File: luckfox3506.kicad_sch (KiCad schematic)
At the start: 3 parts, among them J1 Conn_01x60, J2 Conn_01x60

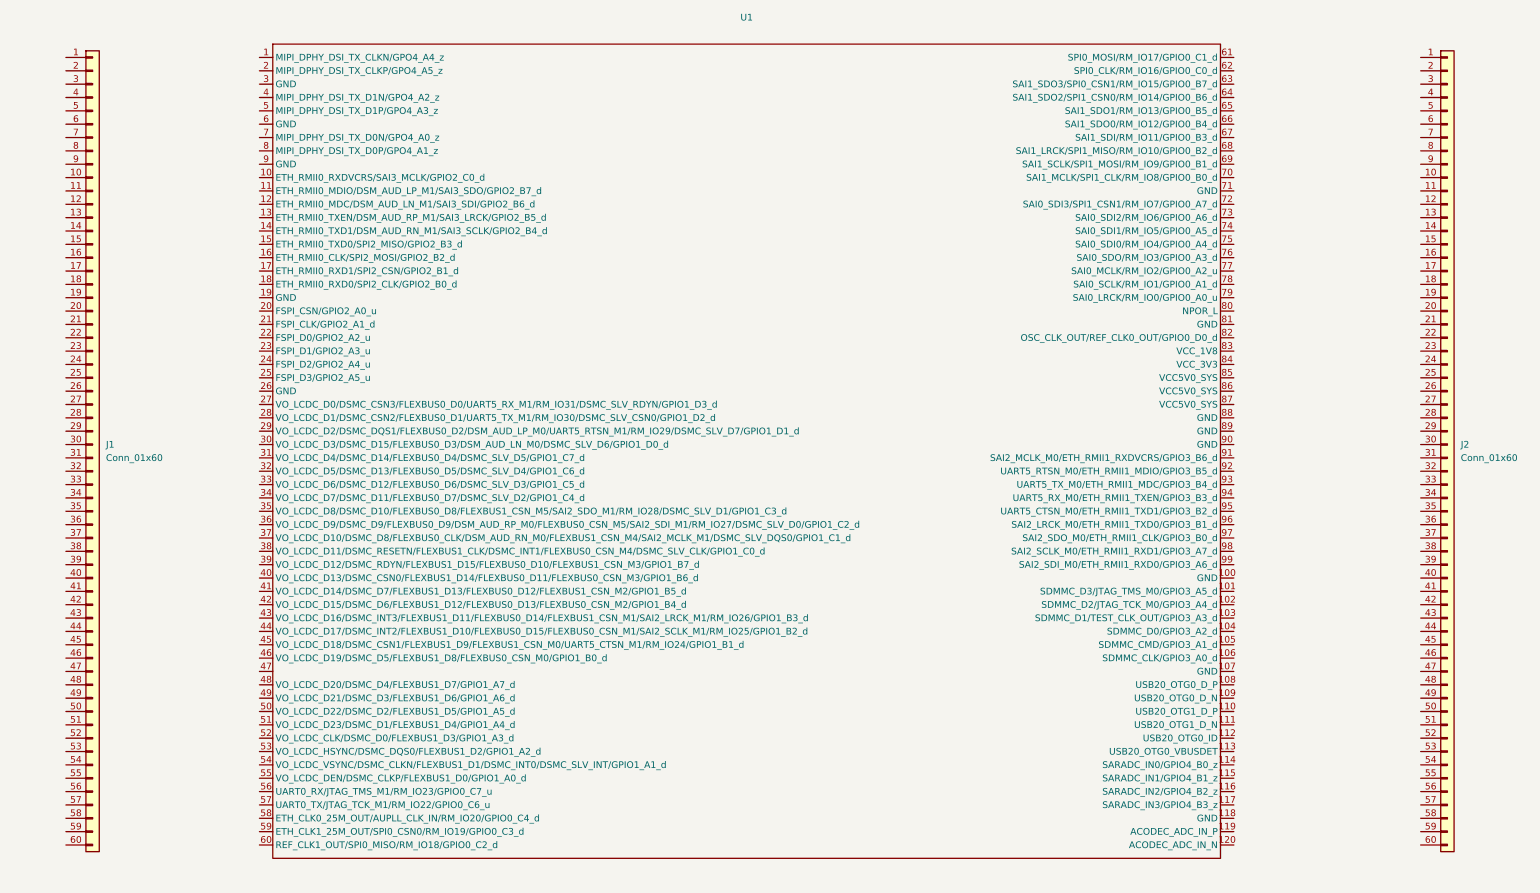
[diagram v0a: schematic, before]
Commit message: Added footprints for headers
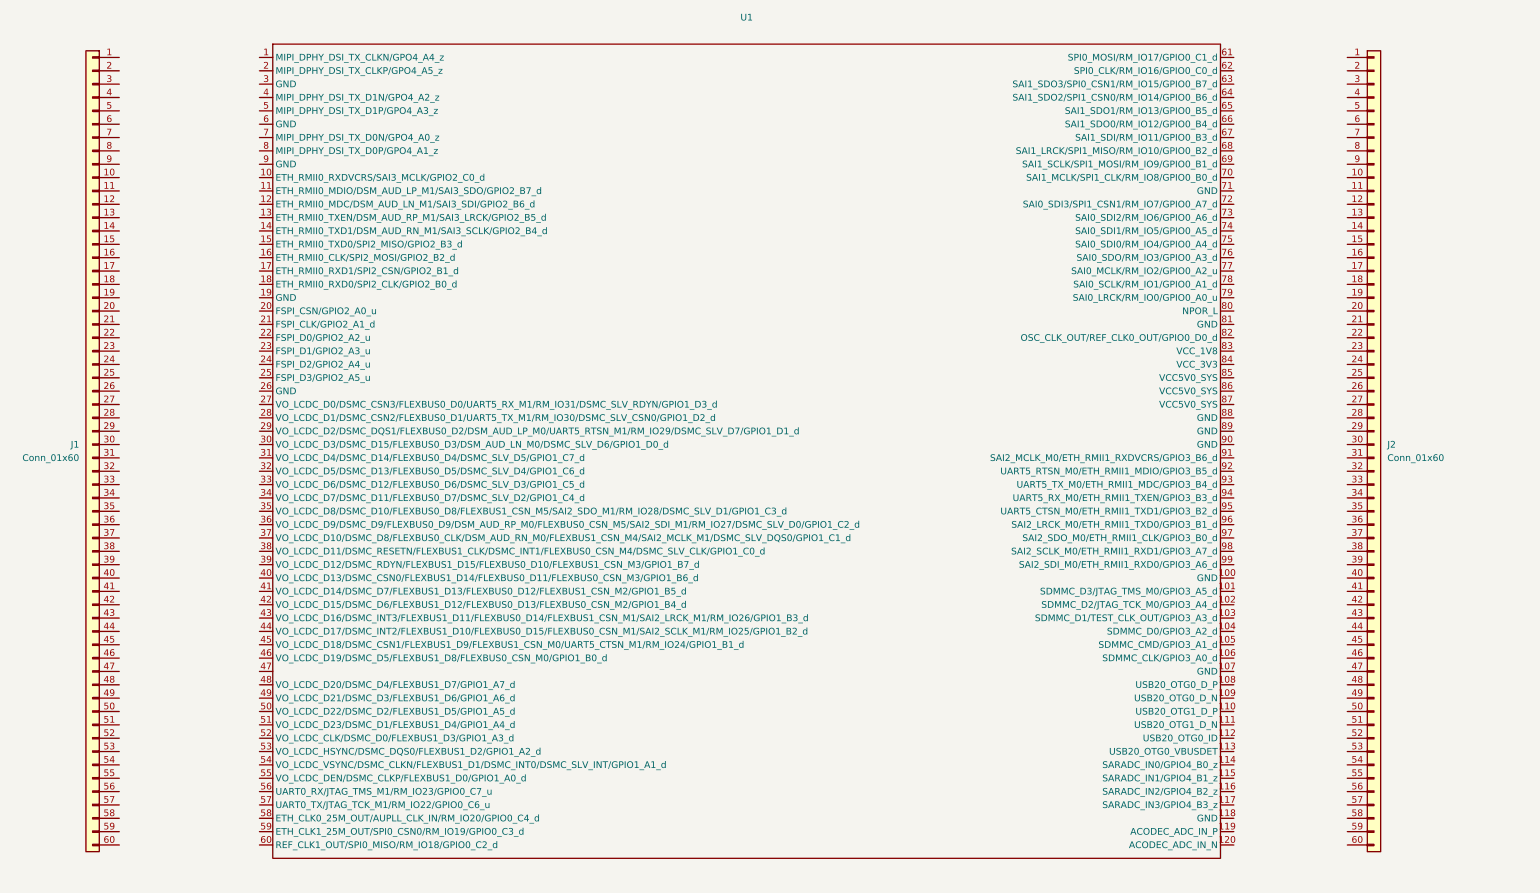
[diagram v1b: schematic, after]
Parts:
- J1, J2: footprint (none) -> Library:PinHeader_1x60_P2.54mm_Vertical
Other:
- moved on the sheet: J1

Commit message: Added nets
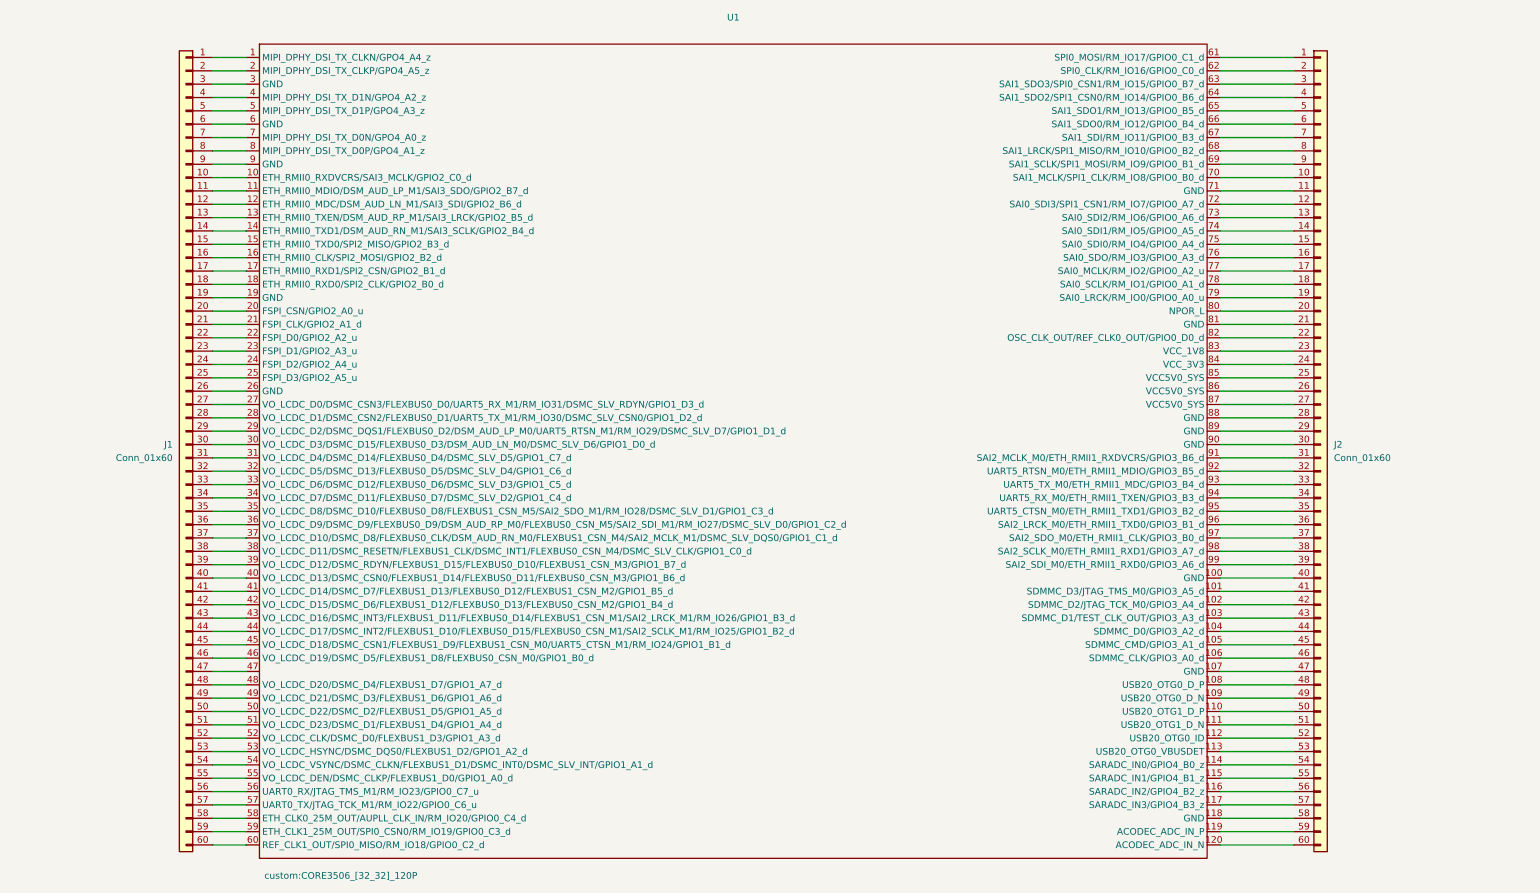
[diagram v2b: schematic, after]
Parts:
- U1: footprint Core3506:CORE3506_[32_32]_120P -> custom:CORE3506_[32_32]_120P
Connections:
- net at J1.1 (Pin_1): now also U1.1 (MIPI_DPHY_DSI_TX_CLKN/GPO4_A4_z)
- net at J1.10 (Pin_10): now also U1.10 (ETH_RMII0_RXDVCRS/SAI3_MCLK/GPIO2_C0_d)
- net at J1.11 (Pin_11): now also U1.11 (ETH_RMII0_MDIO/DSM_AUD_LP_M1/SAI3_SDO/GPIO2_B7_d)
- net at J1.12 (Pin_12): now also U1.12 (ETH_RMII0_MDC/DSM_AUD_LN_M1/SAI3_SDI/GPIO2_B6_d)
- net at J1.13 (Pin_13): now also U1.13 (ETH_RMII0_TXEN/DSM_AUD_RP_M1/SAI3_LRCK/GPIO2_B5_d)
- net at J1.14 (Pin_14): now also U1.14 (ETH_RMII0_TXD1/DSM_AUD_RN_M1/SAI3_SCLK/GPIO2_B4_d)
- net at J1.15 (Pin_15): now also U1.15 (ETH_RMII0_TXD0/SPI2_MISO/GPIO2_B3_d)
- net at J1.16 (Pin_16): now also U1.16 (ETH_RMII0_CLK/SPI2_MOSI/GPIO2_B2_d)
- net at J1.17 (Pin_17): now also U1.17 (ETH_RMII0_RXD1/SPI2_CSN/GPIO2_B1_d)
- net at J1.18 (Pin_18): now also U1.18 (ETH_RMII0_RXD0/SPI2_CLK/GPIO2_B0_d)
- net at J1.19 (Pin_19): now also U1.19 (GND)
- net at J1.2 (Pin_2): now also U1.2 (MIPI_DPHY_DSI_TX_CLKP/GPO4_A5_z)
- net at J1.20 (Pin_20): now also U1.20 (FSPI_CSN/GPIO2_A0_u)
- net at J1.21 (Pin_21): now also U1.21 (FSPI_CLK/GPIO2_A1_d)
- net at J1.22 (Pin_22): now also U1.22 (FSPI_D0/GPIO2_A2_u)
- net at J1.23 (Pin_23): now also U1.23 (FSPI_D1/GPIO2_A3_u)
- net at J1.24 (Pin_24): now also U1.24 (FSPI_D2/GPIO2_A4_u)
- net at J1.25 (Pin_25): now also U1.25 (FSPI_D3/GPIO2_A5_u)
- net at J1.26 (Pin_26): now also U1.26 (GND)
- net at J1.27 (Pin_27): now also U1.27 (VO_LCDC_D0/DSMC_CSN3/FLEXBUS0_D0/UART5_RX_M1/RM_IO31/DSMC_SLV_RDYN/GPIO1_D3_d)
- net at J1.28 (Pin_28): now also U1.28 (VO_LCDC_D1/DSMC_CSN2/FLEXBUS0_D1/UART5_TX_M1/RM_IO30/DSMC_SLV_CSN0/GPIO1_D2_d)
- net at J1.29 (Pin_29): now also U1.29 (VO_LCDC_D2/DSMC_DQS1/FLEXBUS0_D2/DSM_AUD_LP_M0/UART5_RTSN_M1/RM_IO29/DSMC_SLV_D7/GPIO1_D1_d)
- net at J1.3 (Pin_3): now also U1.3 (GND)
- net at J1.30 (Pin_30): now also U1.30 (VO_LCDC_D3/DSMC_D15/FLEXBUS0_D3/DSM_AUD_LN_M0/DSMC_SLV_D6/GPIO1_D0_d)
- net at J1.31 (Pin_31): now also U1.31 (VO_LCDC_D4/DSMC_D14/FLEXBUS0_D4/DSMC_SLV_D5/GPIO1_C7_d)
- net at J1.32 (Pin_32): now also U1.32 (VO_LCDC_D5/DSMC_D13/FLEXBUS0_D5/DSMC_SLV_D4/GPIO1_C6_d)
- net at J1.33 (Pin_33): now also U1.33 (VO_LCDC_D6/DSMC_D12/FLEXBUS0_D6/DSMC_SLV_D3/GPIO1_C5_d)
- net at J1.34 (Pin_34): now also U1.34 (VO_LCDC_D7/DSMC_D11/FLEXBUS0_D7/DSMC_SLV_D2/GPIO1_C4_d)
- net at J1.35 (Pin_35): now also U1.35 (VO_LCDC_D8/DSMC_D10/FLEXBUS0_D8/FLEXBUS1_CSN_M5/SAI2_SDO_M1/RM_IO28/DSMC_SLV_D1/GPIO1_C3_d)
- net at J1.36 (Pin_36): now also U1.36 (VO_LCDC_D9/DSMC_D9/FLEXBUS0_D9/DSM_AUD_RP_M0/FLEXBUS0_CSN_M5/SAI2_SDI_M1/RM_IO27/DSMC_SLV_D0/GPIO1_C2_d)
- net at J1.37 (Pin_37): now also U1.37 (VO_LCDC_D10/DSMC_D8/FLEXBUS0_CLK/DSM_AUD_RN_M0/FLEXBUS1_CSN_M4/SAI2_MCLK_M1/DSMC_SLV_DQS0/GPIO1_C1_d)
- net at J1.38 (Pin_38): now also U1.38 (VO_LCDC_D11/DSMC_RESETN/FLEXBUS1_CLK/DSMC_INT1/FLEXBUS0_CSN_M4/DSMC_SLV_CLK/GPIO1_C0_d)
- net at J1.39 (Pin_39): now also U1.39 (VO_LCDC_D12/DSMC_RDYN/FLEXBUS1_D15/FLEXBUS0_D10/FLEXBUS1_CSN_M3/GPIO1_B7_d)
- net at J1.4 (Pin_4): now also U1.4 (MIPI_DPHY_DSI_TX_D1N/GPO4_A2_z)
- net at J1.40 (Pin_40): now also U1.40 (VO_LCDC_D13/DSMC_CSN0/FLEXBUS1_D14/FLEXBUS0_D11/FLEXBUS0_CSN_M3/GPIO1_B6_d)
- net at J1.41 (Pin_41): now also U1.41 (VO_LCDC_D14/DSMC_D7/FLEXBUS1_D13/FLEXBUS0_D12/FLEXBUS1_CSN_M2/GPIO1_B5_d)
- net at J1.42 (Pin_42): now also U1.42 (VO_LCDC_D15/DSMC_D6/FLEXBUS1_D12/FLEXBUS0_D13/FLEXBUS0_CSN_M2/GPIO1_B4_d)
- net at J1.43 (Pin_43): now also U1.43 (VO_LCDC_D16/DSMC_INT3/FLEXBUS1_D11/FLEXBUS0_D14/FLEXBUS1_CSN_M1/SAI2_LRCK_M1/RM_IO26/GPIO1_B3_d)
- net at J1.44 (Pin_44): now also U1.44 (VO_LCDC_D17/DSMC_INT2/FLEXBUS1_D10/FLEXBUS0_D15/FLEXBUS0_CSN_M1/SAI2_SCLK_M1/RM_IO25/GPIO1_B2_d)
- net at J1.45 (Pin_45): now also U1.45 (VO_LCDC_D18/DSMC_CSN1/FLEXBUS1_D9/FLEXBUS1_CSN_M0/UART5_CTSN_M1/RM_IO24/GPIO1_B1_d)
- net at J1.46 (Pin_46): now also U1.46 (VO_LCDC_D19/DSMC_D5/FLEXBUS1_D8/FLEXBUS0_CSN_M0/GPIO1_B0_d)
- net at J1.47 (Pin_47): now also U1.47
- net at J1.48 (Pin_48): now also U1.48 (VO_LCDC_D20/DSMC_D4/FLEXBUS1_D7/GPIO1_A7_d)
- net at J1.49 (Pin_49): now also U1.49 (VO_LCDC_D21/DSMC_D3/FLEXBUS1_D6/GPIO1_A6_d)
- net at J1.5 (Pin_5): now also U1.5 (MIPI_DPHY_DSI_TX_D1P/GPO4_A3_z)
- net at J1.50 (Pin_50): now also U1.50 (VO_LCDC_D22/DSMC_D2/FLEXBUS1_D5/GPIO1_A5_d)
- net at J1.51 (Pin_51): now also U1.51 (VO_LCDC_D23/DSMC_D1/FLEXBUS1_D4/GPIO1_A4_d)
- net at J1.52 (Pin_52): now also U1.52 (VO_LCDC_CLK/DSMC_D0/FLEXBUS1_D3/GPIO1_A3_d)
- net at J1.53 (Pin_53): now also U1.53 (VO_LCDC_HSYNC/DSMC_DQS0/FLEXBUS1_D2/GPIO1_A2_d)
- net at J1.54 (Pin_54): now also U1.54 (VO_LCDC_VSYNC/DSMC_CLKN/FLEXBUS1_D1/DSMC_INT0/DSMC_SLV_INT/GPIO1_A1_d)
- net at J1.55 (Pin_55): now also U1.55 (VO_LCDC_DEN/DSMC_CLKP/FLEXBUS1_D0/GPIO1_A0_d)
- net at J1.56 (Pin_56): now also U1.56 (UART0_RX/JTAG_TMS_M1/RM_IO23/GPIO0_C7_u)
- net at J1.57 (Pin_57): now also U1.57 (UART0_TX/JTAG_TCK_M1/RM_IO22/GPIO0_C6_u)
- net at J1.58 (Pin_58): now also U1.58 (ETH_CLK0_25M_OUT/AUPLL_CLK_IN/RM_IO20/GPIO0_C4_d)
- net at J1.59 (Pin_59): now also U1.59 (ETH_CLK1_25M_OUT/SPI0_CSN0/RM_IO19/GPIO0_C3_d)
- net at J1.6 (Pin_6): now also U1.6 (GND)
- net at J1.60 (Pin_60): now also U1.60 (REF_CLK1_OUT/SPI0_MISO/RM_IO18/GPIO0_C2_d)
- net at J1.7 (Pin_7): now also U1.7 (MIPI_DPHY_DSI_TX_D0N/GPO4_A0_z)
- net at J1.8 (Pin_8): now also U1.8 (MIPI_DPHY_DSI_TX_D0P/GPO4_A1_z)
- net at J1.9 (Pin_9): now also U1.9 (GND)
- net at J2.1 (Pin_1): now also U1.61 (SPI0_MOSI/RM_IO17/GPIO0_C1_d)
- net at J2.10 (Pin_10): now also U1.70 (SAI1_MCLK/SPI1_CLK/RM_IO8/GPIO0_B0_d)
- net at J2.11 (Pin_11): now also U1.71 (GND)
- net at J2.12 (Pin_12): now also U1.72 (SAI0_SDI3/SPI1_CSN1/RM_IO7/GPIO0_A7_d)
- net at J2.13 (Pin_13): now also U1.73 (SAI0_SDI2/RM_IO6/GPIO0_A6_d)
- net at J2.14 (Pin_14): now also U1.74 (SAI0_SDI1/RM_IO5/GPIO0_A5_d)
- net at J2.15 (Pin_15): now also U1.75 (SAI0_SDI0/RM_IO4/GPIO0_A4_d)
- net at J2.16 (Pin_16): now also U1.76 (SAI0_SDO/RM_IO3/GPIO0_A3_d)
- net at J2.17 (Pin_17): now also U1.77 (SAI0_MCLK/RM_IO2/GPIO0_A2_u)
- net at J2.18 (Pin_18): now also U1.78 (SAI0_SCLK/RM_IO1/GPIO0_A1_d)
- net at J2.19 (Pin_19): now also U1.79 (SAI0_LRCK/RM_IO0/GPIO0_A0_u)
- net at J2.2 (Pin_2): now also U1.62 (SPI0_CLK/RM_IO16/GPIO0_C0_d)
- net at J2.20 (Pin_20): now also U1.80 (NPOR_L)
- net at J2.21 (Pin_21): now also U1.81 (GND)
- net at J2.22 (Pin_22): now also U1.82 (OSC_CLK_OUT/REF_CLK0_OUT/GPIO0_D0_d)
- net at J2.23 (Pin_23): now also U1.83 (VCC_1V8)
- net at J2.24 (Pin_24): now also U1.84 (VCC_3V3)
- net at J2.25 (Pin_25): now also U1.85 (VCC5V0_SYS)
- net at J2.26 (Pin_26): now also U1.86 (VCC5V0_SYS)
- net at J2.27 (Pin_27): now also U1.87 (VCC5V0_SYS)
- net at J2.28 (Pin_28): now also U1.88 (GND)
- net at J2.29 (Pin_29): now also U1.89 (GND)
- net at J2.3 (Pin_3): now also U1.63 (SAI1_SDO3/SPI0_CSN1/RM_IO15/GPIO0_B7_d)
- net at J2.30 (Pin_30): now also U1.90 (GND)
- net at J2.31 (Pin_31): now also U1.91 (SAI2_MCLK_M0/ETH_RMII1_RXDVCRS/GPIO3_B6_d)
- net at J2.32 (Pin_32): now also U1.92 (UART5_RTSN_M0/ETH_RMII1_MDIO/GPIO3_B5_d)
- net at J2.33 (Pin_33): now also U1.93 (UART5_TX_M0/ETH_RMII1_MDC/GPIO3_B4_d)
- net at J2.34 (Pin_34): now also U1.94 (UART5_RX_M0/ETH_RMII1_TXEN/GPIO3_B3_d)
- net at J2.35 (Pin_35): now also U1.95 (UART5_CTSN_M0/ETH_RMII1_TXD1/GPIO3_B2_d)
- net at J2.36 (Pin_36): now also U1.96 (SAI2_LRCK_M0/ETH_RMII1_TXD0/GPIO3_B1_d)
- net at J2.37 (Pin_37): now also U1.97 (SAI2_SDO_M0/ETH_RMII1_CLK/GPIO3_B0_d)
- net at J2.38 (Pin_38): now also U1.98 (SAI2_SCLK_M0/ETH_RMII1_RXD1/GPIO3_A7_d)
- net at J2.39 (Pin_39): now also U1.99 (SAI2_SDI_M0/ETH_RMII1_RXD0/GPIO3_A6_d)
- net at J2.4 (Pin_4): now also U1.64 (SAI1_SDO2/SPI1_CSN0/RM_IO14/GPIO0_B6_d)
- net at J2.40 (Pin_40): now also U1.100 (GND)
- net at J2.41 (Pin_41): now also U1.101 (SDMMC_D3/JTAG_TMS_M0/GPIO3_A5_d)
- net at J2.42 (Pin_42): now also U1.102 (SDMMC_D2/JTAG_TCK_M0/GPIO3_A4_d)
- net at J2.43 (Pin_43): now also U1.103 (SDMMC_D1/TEST_CLK_OUT/GPIO3_A3_d)
- net at J2.44 (Pin_44): now also U1.104 (SDMMC_D0/GPIO3_A2_d)
- net at J2.45 (Pin_45): now also U1.105 (SDMMC_CMD/GPIO3_A1_d)
- net at J2.46 (Pin_46): now also U1.106 (SDMMC_CLK/GPIO3_A0_d)
- net at J2.47 (Pin_47): now also U1.107 (GND)
- net at J2.48 (Pin_48): now also U1.108 (USB20_OTG0_D_P)
- net at J2.49 (Pin_49): now also U1.109 (USB20_OTG0_D_N)
- net at J2.5 (Pin_5): now also U1.65 (SAI1_SDO1/RM_IO13/GPIO0_B5_d)
- net at J2.50 (Pin_50): now also U1.110 (USB20_OTG1_D_P)
- net at J2.51 (Pin_51): now also U1.111 (USB20_OTG1_D_N)
- net at J2.52 (Pin_52): now also U1.112 (USB20_OTG0_ID)
- net at J2.53 (Pin_53): now also U1.113 (USB20_OTG0_VBUSDET)
- net at J2.54 (Pin_54): now also U1.114 (SARADC_IN0/GPIO4_B0_z)
- net at J2.55 (Pin_55): now also U1.115 (SARADC_IN1/GPIO4_B1_z)
- net at J2.56 (Pin_56): now also U1.116 (SARADC_IN2/GPIO4_B2_z)
- net at J2.57 (Pin_57): now also U1.117 (SARADC_IN3/GPIO4_B3_z)
- net at J2.58 (Pin_58): now also U1.118 (GND)
- net at J2.59 (Pin_59): now also U1.119 (ACODEC_ADC_IN_P)
- net at J2.6 (Pin_6): now also U1.66 (SAI1_SDO0/RM_IO12/GPIO0_B4_d)
- net at J2.60 (Pin_60): now also U1.120 (ACODEC_ADC_IN_N)
- net at J2.7 (Pin_7): now also U1.67 (SAI1_SDI/RM_IO11/GPIO0_B3_d)
- net at J2.8 (Pin_8): now also U1.68 (SAI1_LRCK/SPI1_MISO/RM_IO10/GPIO0_B2_d)
- net at J2.9 (Pin_9): now also U1.69 (SAI1_SCLK/SPI1_MOSI/RM_IO9/GPIO0_B1_d)
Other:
- moved on the sheet: J1, J2, U1
